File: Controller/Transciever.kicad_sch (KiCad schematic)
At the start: 10 parts

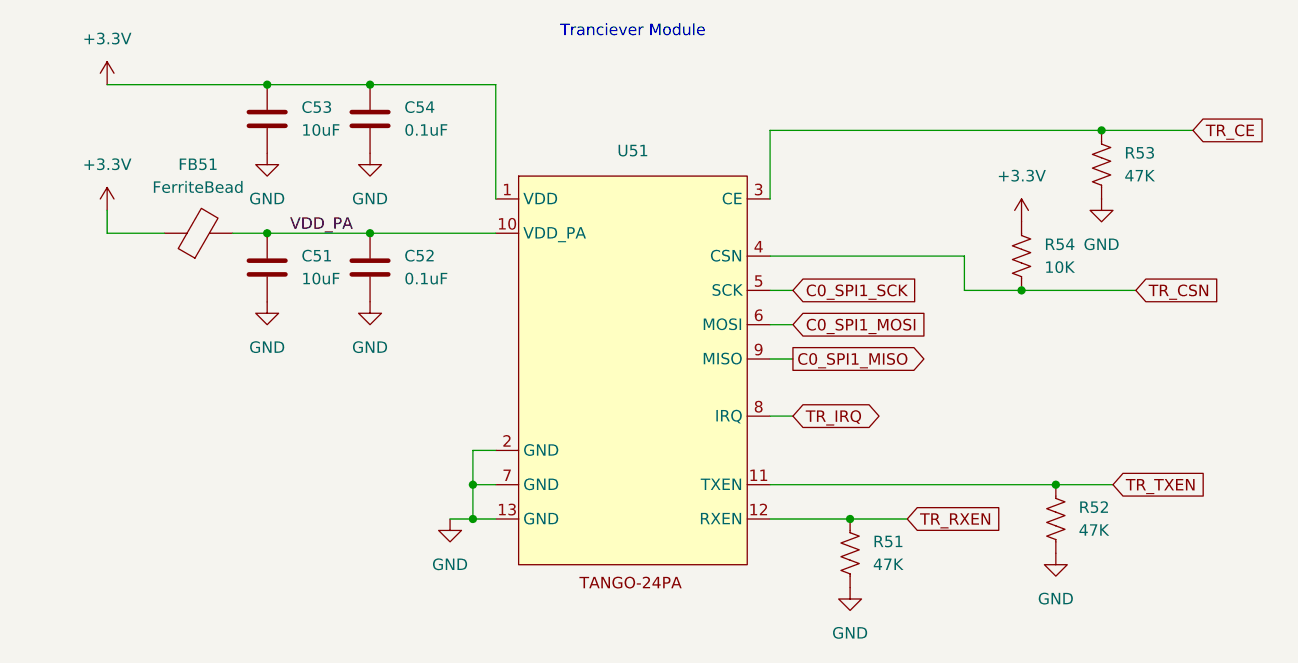
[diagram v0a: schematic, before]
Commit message: Finished Schematic for controller
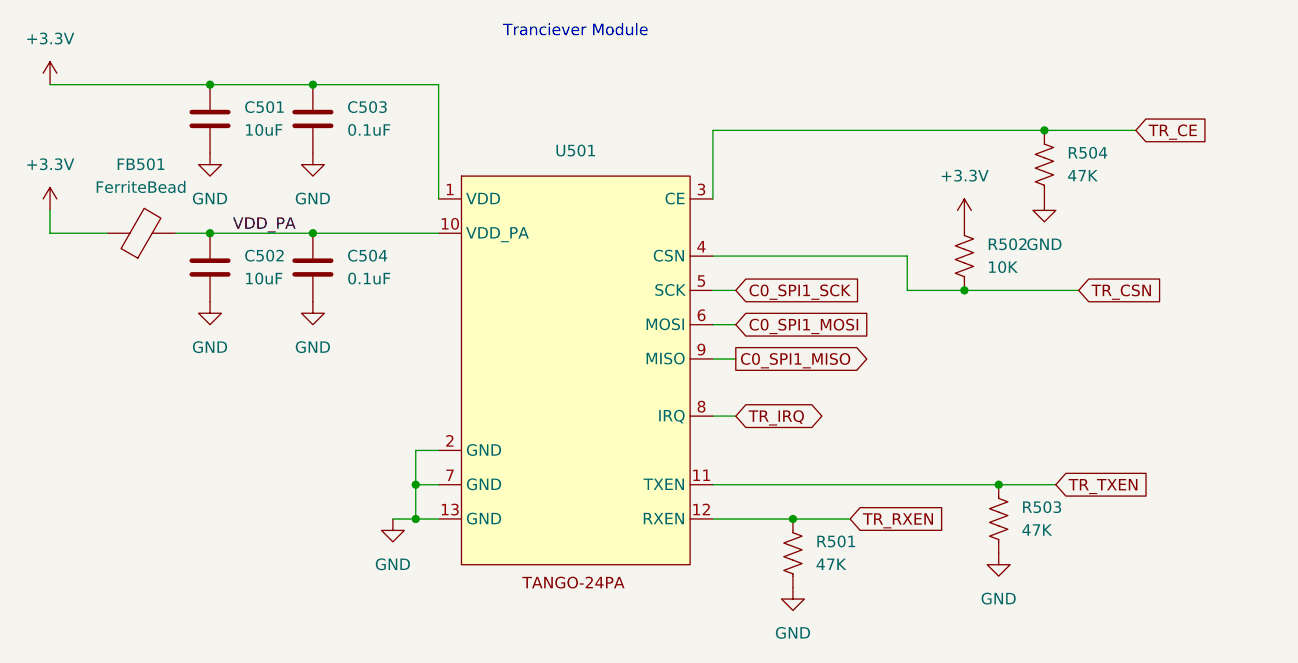
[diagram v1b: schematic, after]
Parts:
- renumbered C53 to C501, C51 to C502, C54 to C503, C52 to C504, FB51 to FB501, R51 to R501, R54 to R502, R52 to R503, R53 to R504, U51 to U501
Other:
- moved on the sheet: C501, C502, C503, C504, FB501, R501, R502, R503, R504, U501
